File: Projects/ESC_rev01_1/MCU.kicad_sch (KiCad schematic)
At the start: 0 parts

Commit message: Update 05
MCU schematic created
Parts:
- added C1, C13: C, symbol Device:C
- added C10, C9: 2u2, symbol Device:C
- added C11, C15, C16, C17, C2, C3, C4, C5, C6, C7, C8: 100n, symbol Device:C
- added C12: 1u, symbol Device:C
- added C14: 10p, symbol Device:C
- added D1, D3: LED_G, symbol Device:LED
- added D2: LED_R, symbol Device:LED
- added FB1: FerriteBead, symbol Device:FerriteBead
- added J1: Conn_01x06, symbol Connector_Generic:Conn_01x06
- added J2: Conn_01x03, symbol Connector_Generic:Conn_01x03
- added J3: Conn_01x08, symbol Connector_Generic:Conn_01x08
- added R1, R3: 0R, symbol Device:R
- added R10: 39k, symbol Device:R
- added R2: R, symbol Device:R
- added R4, R5, R6: 1k, symbol Device:R
- added R7, R8, R9: 2k2, symbol Device:R
- added SW1: SW_DIP_x01, symbol Switch:SW_DIP_x01
- added TH1: 10k, symbol Device:Thermistor_NTC
- added U1: STM32F405RGTx, Package_QFP:LQFP-64_10x10mm_P0.5mm, symbol MCU_ST_STM32F4:STM32F405RGTx
- added Y1: 8M 10ppm, symbol Device:Crystal
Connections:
- new net: D2.2 (A), R5.2
- new net: C11.1, C12.1, FB1.1, U1.13 (VDDA)
- new net: C14.1, R3.1, Y1.2
- new net: C9.1, U1.47 (VCAP_2)
- new net: C13.1, R2.2, Y1.1
- new net: D1.2 (A), R4.2
- new net: J2.3 (Pin_3), R7.2
- new net: C10.1, U1.31 (VCAP_1)
- new net: R1.2, U1.60 (BOOT0)
- new net: D3.2 (A), R6.2
- new net +3V3: C1.1, C16.1, C2.1, C3.1, C4.1, C5.1, C6.1, C7.1, FB1.2, J1.1 (Pin_1), J3.2 (Pin_2), R1.1, R4.1, TH1.1, U1.19 (VDD), U1.32 (VDD), U1.48 (VDD), U1.64 (VDD)
- new net +5V: J2.1 (Pin_1), J3.1 (Pin_1)
- new net +VDC: R10.2
- new net ADC_TEMP: R8.2, TH1.2, U1.17 (PA3)
- new net AN_IN: C17.1, R10.1, R9.2, U1.10 (PC2)
- new net BR_SO1: U1.27 (PB1)
- new net BR_SO2: U1.26 (PB0)
- new net CAN_RX: U1.61 (PB8)
- new net CAN_TX: U1.62 (PB9)
- new net DC_CAL: U1.33 (PB12)
- new net EN_GATE: U1.51 (PC10)
- new net FAULT: U1.53 (PC12)
- new net GND: C1.2, C10.2, C11.2, C12.2, C13.2, C14.2, C15.2, C16.2, C17.2, C2.2, C3.2, C4.2, C5.2, C6.2, C7.2, C8.2, C9.2, D1.1 (K), D2.1 (K), D3.1 (K), J1.3 (Pin_3), J2.2 (Pin_2), J3.3 (Pin_3), J3.8 (Pin_8), R8.1, R9.1, SW1.1, U1.12 (VSSA), U1.18 (VSS), U1.63 (VSS)
- new net H1: U1.43 (PA10)
- new net H2: U1.42 (PA9)
- new net H3: U1.41 (PA8)
- new net HALL_1: U1.58 (PB6)
- new net HALL_2: U1.59 (PB7)
- new net HALL_3: U1.52 (PC11)
- new net L1: U1.36 (PB15)
- new net L2: U1.35 (PB14)
- new net L3: U1.34 (PB13)
- new net LED_GREEN: R6.1, U1.24 (PC4)
- new net LED_RED: R5.1, U1.25 (PC5)
- new net MISO_ADC_EXT2: J3.7 (Pin_7), U1.22 (PA6)
- new net NRST: C8.1, J1.5 (Pin_5), SW1.2, U1.7 (NRST)
- new net PH_0_P: R2.1, U1.5 (PH0)
- new net PH_1_P: R3.2, U1.6 (PH1)
- new net RX_SCL_MOS: U1.23 (PA7)
- new net RX_SCL_MOSI: J3.6 (Pin_6), U1.29 (PB10), U1.38 (PC7)
- new net SCK_ADC_EXT: J3.4 (Pin_4), U1.21 (PA5)
- new net SENS1: U1.16 (PA2)
- new net SENS2: U1.15 (PA1)
- new net SENS3: U1.14 (PA0)
- new net SERVO: C15.1, R7.1, U1.57 (PB5)
- new net SWCLK: J1.2 (Pin_2), U1.49 (PA14)
- new net SWDIO: J1.4 (Pin_4), U1.46 (PA13)
- new net TEMP_MOTOR: U1.8 (PC0)
- new net TX_SDA_NSS: J3.5 (Pin_5), U1.20 (PA4), U1.30 (PB11), U1.37 (PC6)
- new net USB_DM: U1.44 (PA11)
- new net USB_DP: U1.45 (PA12)
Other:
- note added: "100nF Decoupling capacitors. Place one as close as possible to each pin."
- note added: "COMMUNICATION"
- note added: "MCU"
- note added: "NRST internally pulled-up"
- note added: "NTC THERMISTOR"
- note added: "PROGRAMMING/ DEBUG"
- note added: "REPLACE WITH 100R IF USED AS SERVO OUTPUT"
- note added: "SERVO"
- note added: "See Boot Modes Table 7"
- note added: "VOLTAGE_DIVIDER"
- note added: "WHEN: VDC = 60V => AN_IN = 3V204"

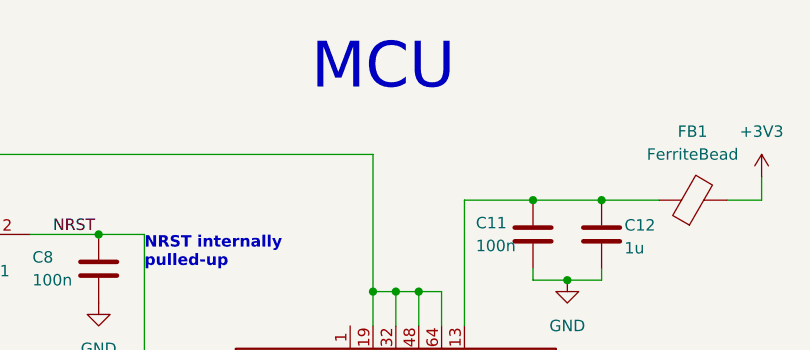
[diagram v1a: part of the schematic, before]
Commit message: Update 06
MOSFET DRIVER schematic created
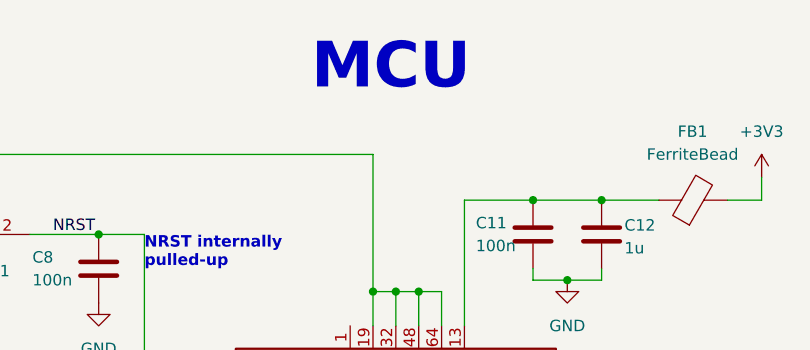
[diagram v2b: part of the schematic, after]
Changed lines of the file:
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@@
 			(font
 				(size 5.08 5.08)
+				(thickness 1.016)
+				(bold yes)
 			)
 			(justify left)

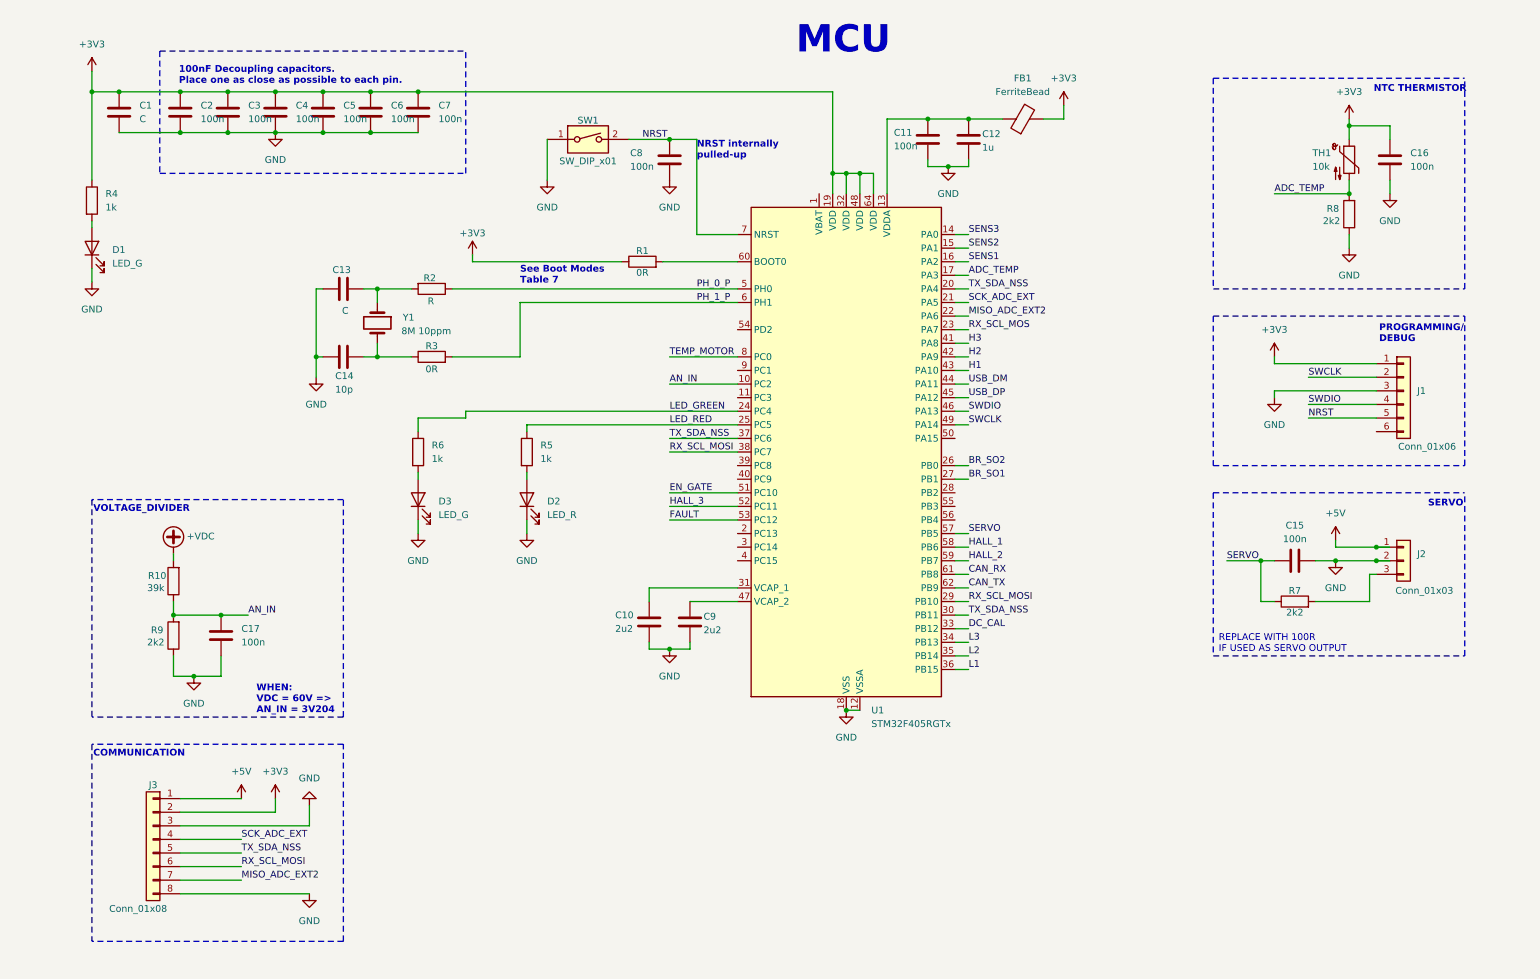
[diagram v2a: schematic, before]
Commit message: Update 07
Schematic is ready
INPUT PROTECTION schematic created
MOSFETs schematic created
CAN schematic created
FILTERs schematic created
MECHANICAL schematic created
STEP-DOWN schematic created
Footprints, 3D models are added and corrected (major issues)
Component placement started
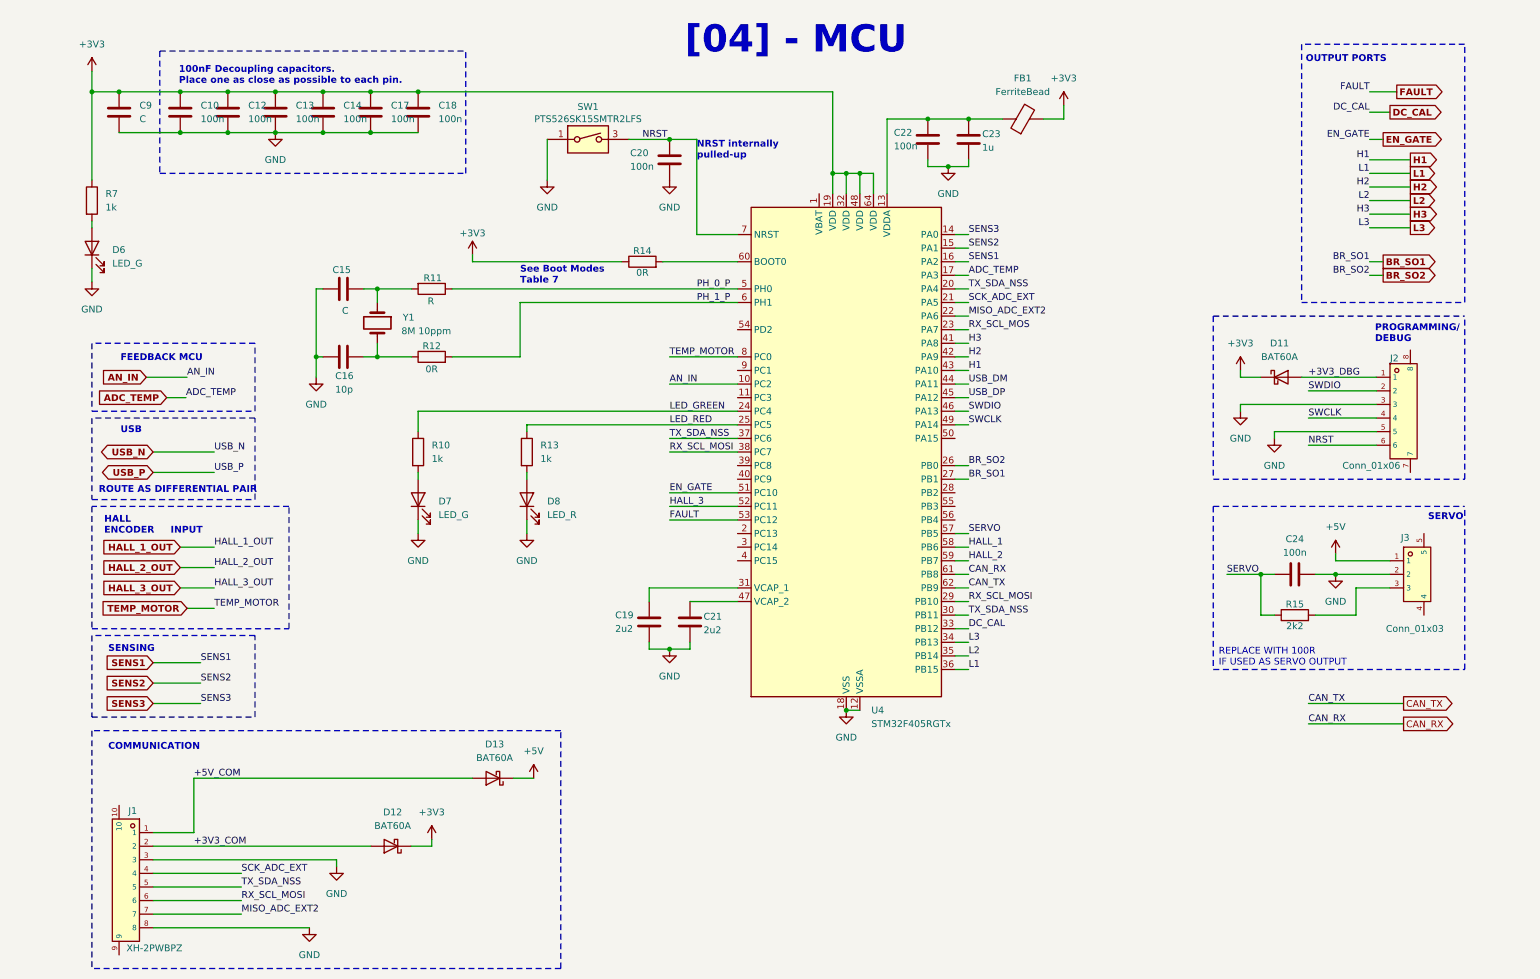
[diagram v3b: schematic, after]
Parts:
- removed C16, C17: 100n, symbol Device:C
- removed R10: 39k, symbol Device:R
- removed R8, R9: 2k2, symbol Device:R
- removed TH1: 10k, symbol Device:Thermistor_NTC
- added D11, D12, D13: BAT60A, Diode_SMD:D_SOD-323, symbol Diode:BAT60A
- C10: renamed from C2; footprint (none) -> Capacitor_SMD:C_0603_1608Metric
- C12: renamed from C3; footprint (none) -> Capacitor_SMD:C_0603_1608Metric
- C13: renamed from C4; footprint (none) -> Capacitor_SMD:C_0603_1608Metric
- C14: renamed from C5; footprint (none) -> Capacitor_SMD:C_0603_1608Metric
- C15: renamed from C13; footprint (none) -> Capacitor_SMD:C_0603_1608Metric
- C16: renamed from C14; footprint (none) -> Capacitor_SMD:C_0603_1608Metric
- C17: renamed from C6; footprint (none) -> Capacitor_SMD:C_0603_1608Metric
- C18: renamed from C7; footprint (none) -> Capacitor_SMD:C_0603_1608Metric
- C19: renamed from C10; footprint (none) -> Capacitor_SMD:C_0603_1608Metric
- C20: renamed from C8; footprint (none) -> Capacitor_SMD:C_0603_1608Metric
- C21: renamed from C9; footprint (none) -> Capacitor_SMD:C_0603_1608Metric
- C22: renamed from C11; footprint (none) -> Capacitor_SMD:C_0603_1608Metric
- C23: renamed from C12; footprint (none) -> Capacitor_SMD:C_0603_1608Metric
- C24: renamed from C15; footprint (none) -> Capacitor_SMD:C_0603_1608Metric
- C9: renamed from C1; footprint (none) -> Capacitor_SMD:C_0603_1608Metric
- D6: renamed from D1; footprint (none) -> LED_SMD:LED_1206_3216Metric
- D7: renamed from D3; footprint (none) -> LED_SMD:LED_1206_3216Metric
- D8: renamed from D2; footprint (none) -> LED_SMD:LED_1206_3216Metric
- FB1: footprint (none) -> Inductor_SMD:L_0603_1608Metric
- J1: renamed from J3; value Conn_01x08 -> XH-2PWBPZ; footprint (none) -> DF_ESC_rev01_1:CONN-SMD_8P-P2.50_HX25003-8AWB; symbol Connector_Generic:Conn_01x08 -> DF_ESC_rev01_1:Conn_01x08_2mnt; LCSC (none) -> C2687444
- J2: renamed from J1; footprint (none) -> DF_ESC_rev01_1:CONN-SMD_6P-P2.50_DEALON_XH-6PWB; symbol Connector_Generic:Conn_01x06 -> XH-2PWBPZ:Conn_01x06_2mnt; LCSC (none) -> C2687444
- J3: renamed from J2; footprint (none) -> DF_ESC_rev01_1:CONN-SMD_XH-3AWB; symbol Connector_Generic:Conn_01x03 -> PUSB3AB6Z:Conn_01x03_2mnt; LCSC (none) -> C141812
- R10: renamed from R6; footprint (none) -> Resistor_SMD:R_0603_1608Metric
- R11: renamed from R2; footprint (none) -> Resistor_SMD:R_0603_1608Metric
- R12: renamed from R3; footprint (none) -> Resistor_SMD:R_0603_1608Metric
- R13: renamed from R5; footprint (none) -> Resistor_SMD:R_0603_1608Metric
- R14: renamed from R1; footprint (none) -> Resistor_SMD:R_0603_1608Metric
- R15: renamed from R7; footprint (none) -> Resistor_SMD:R_0603_1608Metric
- R7: renamed from R4; footprint (none) -> Resistor_SMD:R_0603_1608Metric
- SW1: value SW_DIP_x01 -> PTS526SK15SMTR2LFS; footprint (none) -> DF_ESC_rev01_1:SW-SMD_4P-L5.2-W5.2-P3.70-LS6.4; symbol Switch:SW_DIP_x01 -> PUSB3AB6Z:SW_DIP_x01_4pin
- Y1: footprint (none) -> DF_ESC_rev01_1:CRYSTAL-SMD_L5.0-W3.2
- renumbered U1 to U4
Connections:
- net +3V3: now also D11.1 (K), D12.1 (K); no longer J1.2 (Pin_2), J2.1 (Pin_1)
- net +5V: now also D13.1 (K); no longer J1.1 (Pin_1)
- net GND: now also J2.5, SW1.2
- net NRST: now also J2.6, SW1.3, SW1.4; no longer J2.5 (Pin_5), SW1.2
- net SWCLK: now also J2.4; no longer J2.2 (Pin_2)
- net SWDIO: now also J2.2; no longer J2.4 (Pin_4)
- new net +3V3_COM: D12.2 (A), J1.2
- new net +3V3_DBG: D11.2 (A), J2.1
- new net +5V_COM: D13.2 (A), J1.1
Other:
- note added: "FEEDBACK MCU"
- note added: "HALL ENCODER INPUT"
- note added: "OUTPUT PORTS"
- note added: "ROUTE AS DIFFERENTIAL PAIR"
- note added: "SENSING"
- note added: "USB"
- note added: "[04] - MCU"
- note removed: "MCU"
- note removed: "NTC THERMISTOR"
- note removed: "VOLTAGE_DIVIDER"
- note removed: "WHEN: VDC = 60V => AN_IN = 3V204"
- moved on the sheet: C24, R15

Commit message: Update 09
Components placement finished
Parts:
- removed D6: LED_G, LED_SMD:LED_1206_3216Metric, symbol Device:LED
- removed R7: 1k, Resistor_SMD:R_0603_1608Metric, symbol Device:R
- added D6: PESD3V3X1BL, DF_ESC_rev01_1:D_SOD-882_BI, symbol DF_ESC_rev01_1:PESD3V3X1BL,315
- added D9: SD05C-7, Diode_SMD:D_SOD-323_HandSoldering, symbol DF_ESC_rev01_1:SD05D-7
- added R11: 2k2, Resistor_SMD:R_0603_1608Metric, symbol Device:R
- C14: renamed from C15; value C -> 10p
- C9: value C -> 10u
- R12: renamed from R14; value 0R -> 100R
- R8: renamed from R11; value R -> 0R
- Y1: value 8M 10ppm -> 8M 10ppm X50328MSB2GI
- renumbered C12 to C11, C13 to C12, C14 to C13, C16 to C15, C17 to C16, C18 to C17, C19 to C18, C20 to C19, C21 to C20, C22 to C21, C23 to C22, C24 to C23, D13 to D10, D8 to D11, D11 to D12, D12 to D7, D7 to D8, J1 to J3, J2 to J4, J3 to J5, R13 to R10, R15 to R13, R10 to R7, R12 to R9, U4 to U2
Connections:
- net +3V3: no longer R12.1
- net +3V3_COM: now also D6.2 (A2)
- net +5V_COM: now also D9.2 (A2)
- net GND: now also R12.1, D6.1 (A1), D9.1 (A1), R11.2; no longer SW1.1, SW1.2
- net RX_SCL_MOSI: now also J3.5; no longer J3.6
- net TX_SDA_NSS: now also J3.6; no longer J3.5
- net +3V3_A: now reaches C21.1, C22.1, FB1.1, U2.13 (VDDA)
- net PH_1: now reaches C15.1, R9.1, Y1.2
- net VCAP_2: now reaches C20.1, U2.47 (VCAP_2)
- net PH_0: now reaches C14.1, R8.2, Y1.1
- net VCAP_1: now reaches C18.1, U2.31 (VCAP_1)
- net BOOT: now reaches R12.2, U2.60 (BOOT0)
- new net: R11.1, SW1.1, SW1.2
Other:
- moved on the sheet: D10

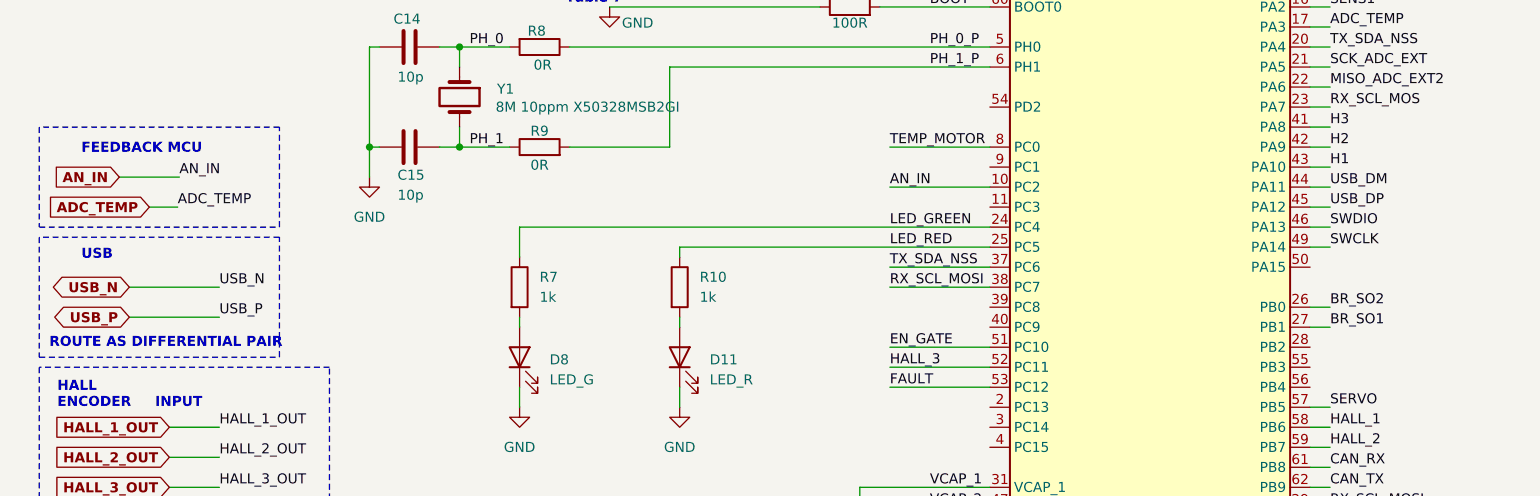
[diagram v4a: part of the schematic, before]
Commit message: Update 11
Draft routing - diff signals and power
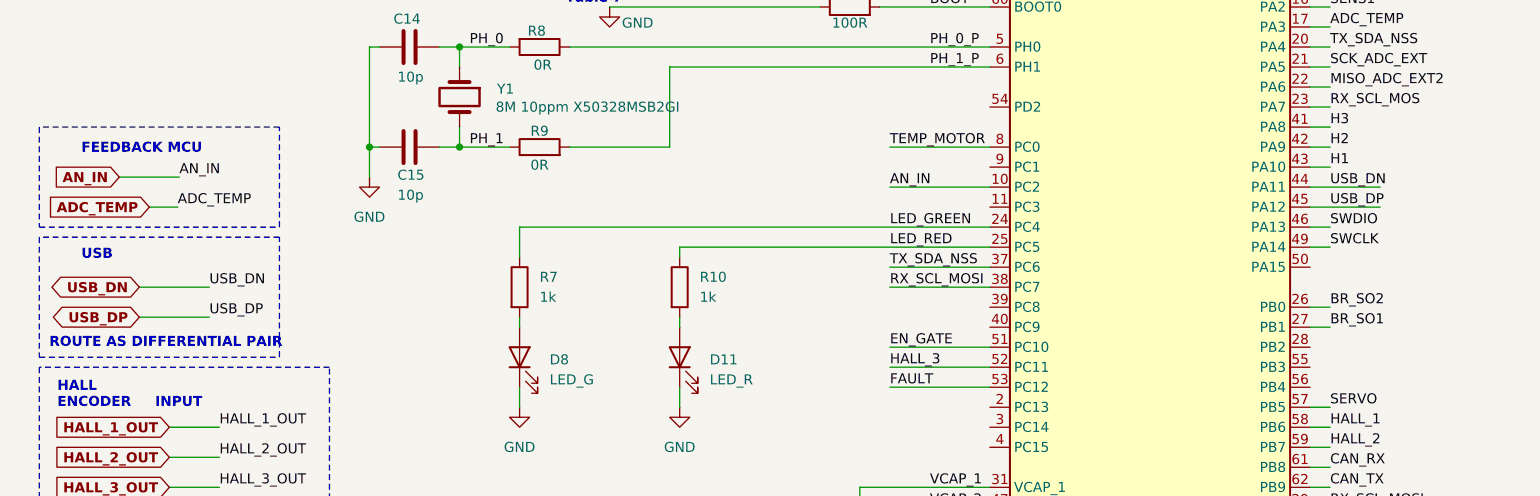
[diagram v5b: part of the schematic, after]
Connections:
- net USB_DM renamed USB_DN
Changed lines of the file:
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@@
-	(wire
-		(pts
-			(xy 184.15 85.09) (xy 181.61 85.09)
-		)
-		(stroke
-			(width 0)
-			(type default)
-		)
-	)
 	(wire
 		(pts
@@
 	(wire
 		(pts
+			(xy 181.61 82.55) (xy 190.5 82.55)
+		)
+		(stroke
+			(width 0)
+			(type default)
+		)
+	)
+	(wire
+		(pts
 			(xy 158.75 43.18) (xy 161.29 43.18)
 		)
@@
 	(wire
 		(pts
-			(xy 31.75 99.06) (xy 43.18 99.06)
+			(xy 33.02 99.06) (xy 41.91 99.06)
 		)
 		(stroke
@@
 	(wire
 		(pts
-			(xy 184.15 82.55) (xy 181.61 82.55)
-		)
-		(stroke
-			(width 0)
-			(type default)
-		)
-	)
-	(wire
-		(pts
 			(xy 184.15 80.01) (xy 181.61 80.01)
 		)
@@
 	(wire
 		(pts
-			(xy 31.75 95.25) (xy 43.18 95.25)
+			(xy 33.02 95.25) (xy 41.91 95.25)
 		)
 		(stroke
@@
 		(pts
 			(xy 128.27 92.71) (xy 140.97 92.71)
+		)
+		(stroke
+			(width 0)
+			(type default)
+		)
+	)
+	(wire
+		(pts
+			(xy 181.61 85.09) (xy 190.5 85.09)
 		)
 		(stroke
@@
 		)
 	)
-	(label "USB_N"
-		(at 43.18 95.25 0)
+	(label "USB_DN"
+		(at 41.91 95.25 0)
 		(effects
 			(font
@@
 		)
 	)
-	(label "USB_DM"
+	(label "USB_DN"
 		(at 184.15 82.55 0)
 		(effects
@@
 		)
 	)
-	(label "USB_P"
-		(at 43.18 99.06 0)
+	(label "USB_DP"
+		(at 41.91 99.06 0)
 		(effects
 			(font
@@
 		)
 	)
-	(global_label "USB_P"
+	(global_label "USB_DP"
 		(shape bidirectional)
-		(at 31.75 99.06 180)
+		(at 33.02 99.06 180)
 		(fields_autoplaced yes)
 		(effects
@@
 		)
 		(property "Intersheetrefs" "${INTERSHEET_REFS}"
-			(at 22.8717 99.06 0)
+			(at 21.1301 99.06 0)
 			(effects
 				(font
@@
 		)
 	)
-	(global_label "USB_N"
+	(global_label "USB_DN"
 		(shape bidirectional)
-		(at 31.75 95.25 180)
+		(at 33.02 95.25 180)
 		(fields_autoplaced yes)
 		(effects
@@
 		)
 		(property "Intersheetrefs" "${INTERSHEET_REFS}"
-			(at 22.8717 95.25 0)
+			(at 21.0696 95.25 0)
 			(effects
 				(font

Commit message: Update 12
Continue routing
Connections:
- net HALL_1 is gone; now on net HALL_1_OUT: U2.58 (PB6)
- net HALL_2 is gone; now on net HALL_2_OUT: U2.59 (PB7)
- net HALL_3 is gone; now on net HALL_3_OUT: U2.52 (PC11)
- net +3V3: now also U2.1 (VBAT)
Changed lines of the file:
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@@
+	(wire
+		(pts
+			(xy 156.21 43.18) (xy 158.75 43.18)
+		)
+		(stroke
+			(width 0)
+			(type default)
+		)
+	)
 	(wire
 		(pts
@@
 		(pts
 			(xy 63.5 27.94) (xy 72.39 27.94)
+		)
+		(stroke
+			(width 0)
+			(type default)
+		)
+	)
+	(wire
+		(pts
+			(xy 156.21 46.99) (xy 156.21 43.18)
 		)
 		(stroke
@@
 		)
 	)
-	(label "HALL_2"
+	(label "HALL_2_OUT"
 		(at 184.15 115.57 0)
 		(effects
@@
 		)
 	)
-	(label "HALL_1"
+	(label "HALL_1_OUT"
 		(at 184.15 113.03 0)
 		(effects
@@
 		)
 	)
-	(label "HALL_3"
+	(label "HALL_3_OUT"
 		(at 128.27 105.41 0)
 		(effects
